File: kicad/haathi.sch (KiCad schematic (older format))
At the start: 0 parts

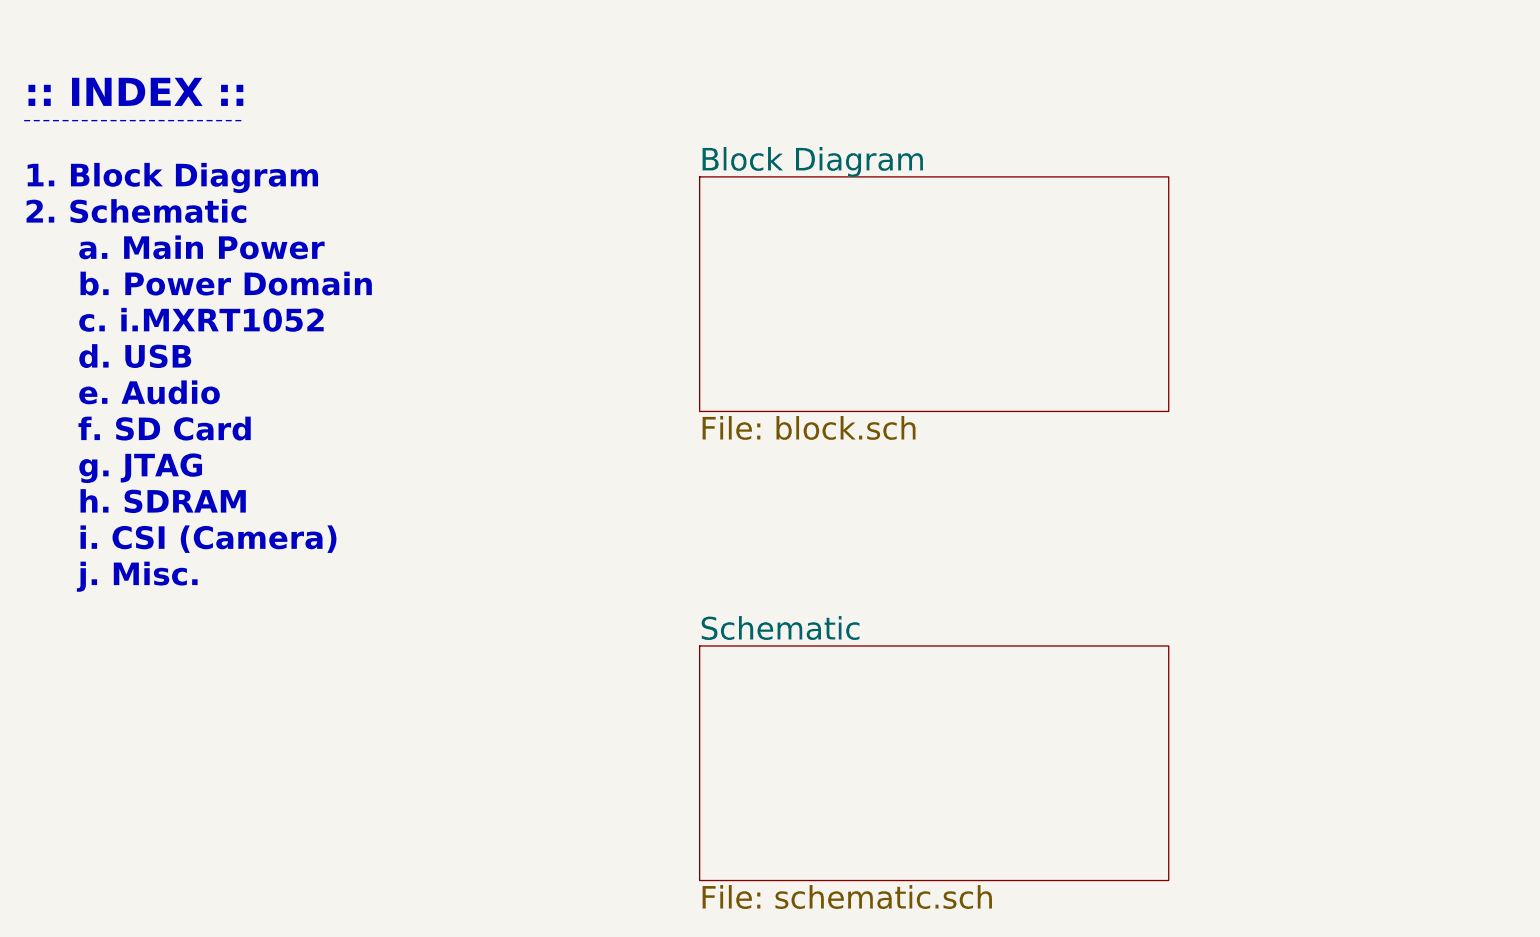
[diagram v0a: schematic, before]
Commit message: created schematic structure
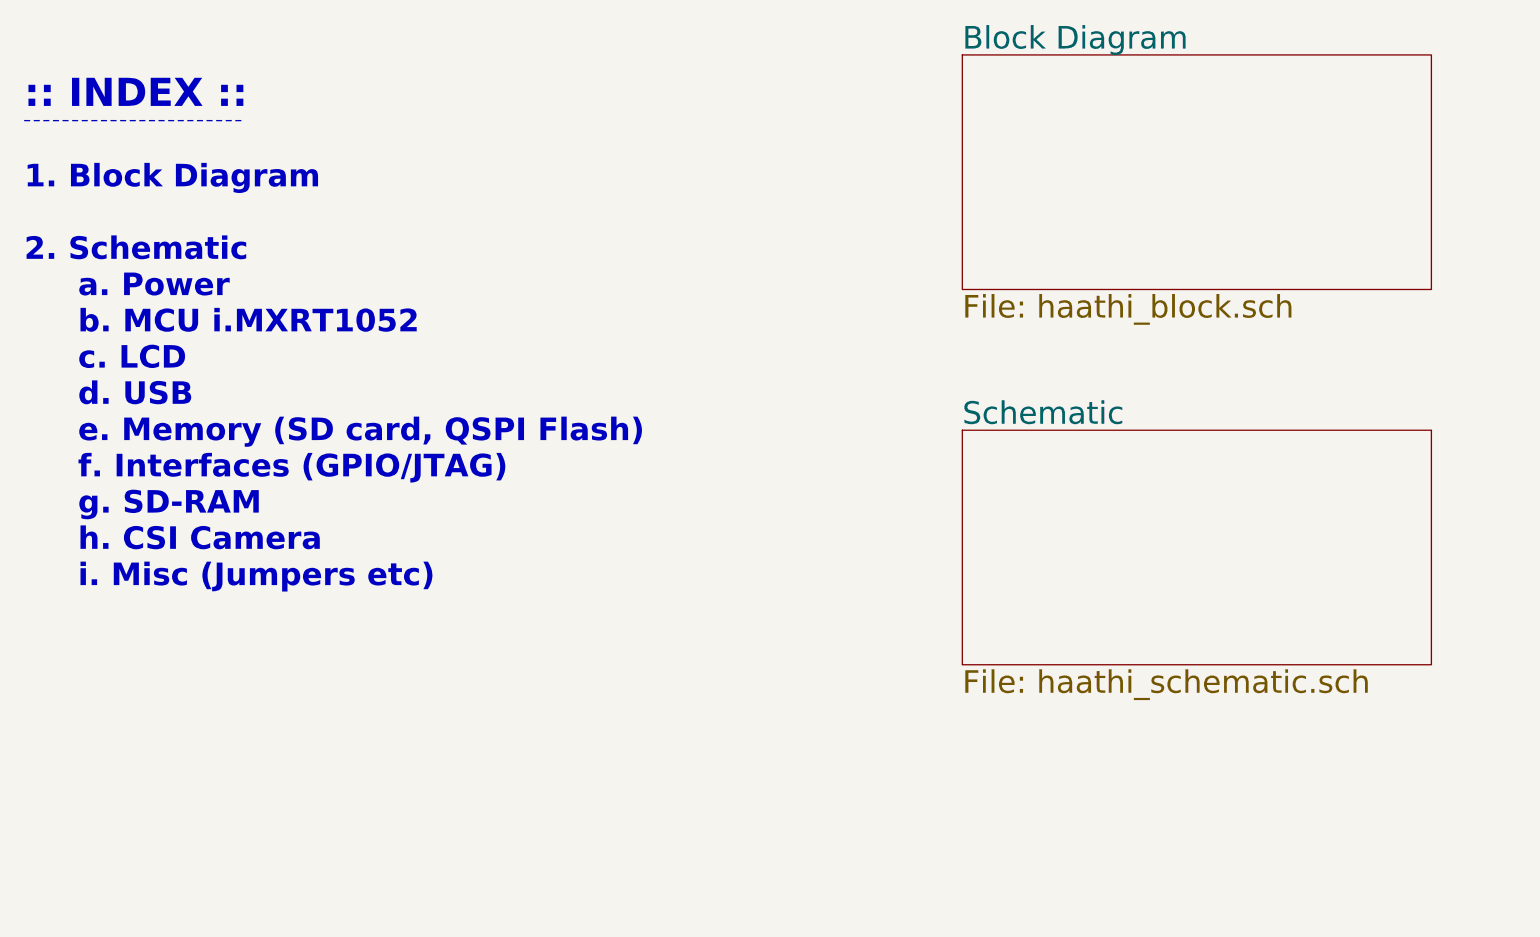
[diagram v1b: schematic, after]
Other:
- note added: "1. Block Diagram\n\n2. Schematic\n a. Power\n b. MCU i.MXRT1052\n c. LCD\n d. USB\n e. Memory (SD card, QSPI Flash)\n f. Interfaces (GPIO/JTAG)\n g. SD-RAM\n h. CSI Camera\n i. Misc (Jumpers etc)"
- note removed: "1. Block Diagram\n2. Schematic\n a. Main Power\n b. Power Domain\n c. i.MXRT1052\n d. USB\n e. Audio\n f. SD Card\n g. JTAG\n h. SDRAM\n i. CSI (Camera)\n j. Misc."
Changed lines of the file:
@@
 $Descr A4 11693 8268
 encoding utf-8
-Sheet 1 3
+Sheet 1 12
 Title ""
 Date "2018-01-04"
@@
 	1400 1200 2575 1200
 Text Notes 1400 3700 0    120  ~ 24
-1. Block Diagram\n2. Schematic\n     a. Main Power\n     b. Power Domain\n     c. i.MXRT1052\n     d. USB\n     e. Audio\n     f. SD Card\n     g. JTAG\n     h. SDRAM\n     i. CSI (Camera)\n     j. Misc.
+1. Block Diagram\n\n2. Schematic\n     a. Power\n     b. MCU i.MXRT1052\n     c. LCD\n     d. USB\n     e. Memory (SD card, QSPI Flash)\n     f. Interfaces (GPIO/JTAG)\n     g. SD-RAM\n     h. CSI Camera\n     i. Misc (Jumpers etc)
 $Sheet
-S 5000 1500 2500 1250
+S 6400 850  2500 1250
 U 5A56B6F6
 F0 "Block Diagram" 120
-F1 "block.sch" 120
+F1 "haathi_block.sch" 120
 $EndSheet
 $Sheet
-S 5000 4000 2500 1250
+S 6400 2850 2500 1250
 U 5A56B6FF
 F0 "Schematic" 120
-F1 "schematic.sch" 120
+F1 "haathi_schematic.sch" 120
 $EndSheet
 $EndSCHEMATC

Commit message: Overview sheet, added Google Sheet and Gitter links
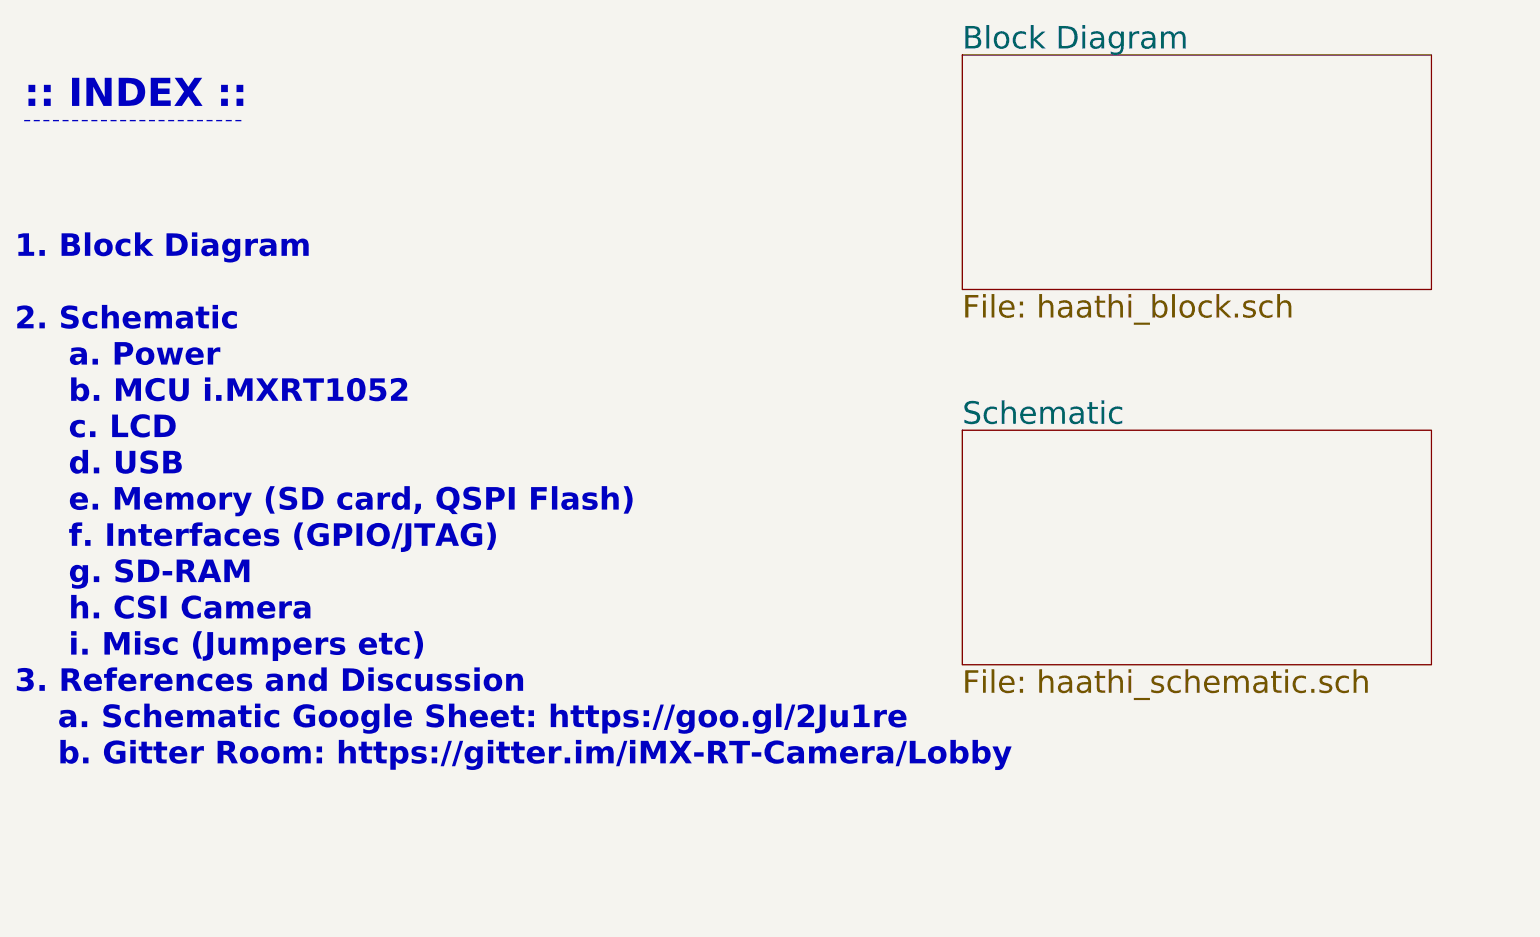
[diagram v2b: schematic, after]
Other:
- note added: "1. Block Diagram\n\n2. Schematic\n a. Power\n b. MCU i.MXRT1052\n c. LCD\n d. USB\n e. Memory (SD card, QSPI Flash)\n f. Interfaces (GPIO/JTAG)\n g. SD-RAM\n h. CSI Camera\n i. Misc (Jumpers etc)\n3. References and Discussion\n a. Schematic Google Sheet: https://goo.gl/2Ju1re\n b. Gitter Room: https://gitter.im/iMX-RT-Camera/Lobby"
- note removed: "1. Block Diagram\n\n2. Schematic\n a. Power\n b. MCU i.MXRT1052\n c. LCD\n d. USB\n e. Memory (SD card, QSPI Flash)\n f. Interfaces (GPIO/JTAG)\n g. SD-RAM\n h. CSI Camera\n i. Misc (Jumpers etc)"
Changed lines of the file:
@@
 Wire Notes Line
 	1400 1200 2575 1200
-Text Notes 1400 3700 0    120  ~ 24
-1. Block Diagram\n\n2. Schematic\n     a. Power\n     b. MCU i.MXRT1052\n     c. LCD\n     d. USB\n     e. Memory (SD card, QSPI Flash)\n     f. Interfaces (GPIO/JTAG)\n     g. SD-RAM\n     h. CSI Camera\n     i. Misc (Jumpers etc)
+Text Notes 1350 4650 0    120  ~ 24
+1. Block Diagram\n\n2. Schematic\n     a. Power\n     b. MCU i.MXRT1052\n     c. LCD\n     d. USB\n     e. Memory (SD card, QSPI Flash)\n     f. Interfaces (GPIO/JTAG)\n     g. SD-RAM\n     h. CSI Camera\n     i. Misc (Jumpers etc)\n3. References and Discussion\n    a. Schematic Google Sheet: https://goo.gl/2Ju1re\n    b. Gitter Room: https://gitter.im/iMX-RT-Camera/Lobby
 $Sheet
 S 6400 850  2500 1250
